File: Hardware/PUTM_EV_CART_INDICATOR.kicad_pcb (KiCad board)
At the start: 2 copper layers, 43 x 25 mm, 17 parts, among them J1 Screw_Terminal_01x08, K3 IM07DTS, K4 IM07DTS

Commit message: poprawy diod
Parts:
- moved D1 10.8 mm to (112.0, 72.0), turned to 0 degrees
- moved D2 6.40 mm to (102.0, 72.0), turned to 0 degrees
- moved K4 1.80 mm to (111.9, 79.3), turned to -90 degrees
- moved K3 1.60 mm to (101.9, 79.1)
- moved H1 1.00 mm to (85.0, 80.0)
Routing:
- net Net-(D1-A): track 16.0 -> 8.33 mm
- net Net-(K4-NC_2): track 11.0 -> 4.48 mm
- net +24V: track 49.4 -> 51.5 mm
- net Net-(D2-A): track 13.0 -> 14.6 mm, vias 0 -> 1
- net Net-(K3-NO_1): track 3.87 -> 5.11 mm
- net /TSAL_COLUMN: track 33.5 -> 34.1 mm
- net /IMD_COLUMN: track 18.8 -> 18.2 mm
- net GND: vias 8 -> 12
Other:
- board size 43 x 25 mm -> 43 x 26.5 mm

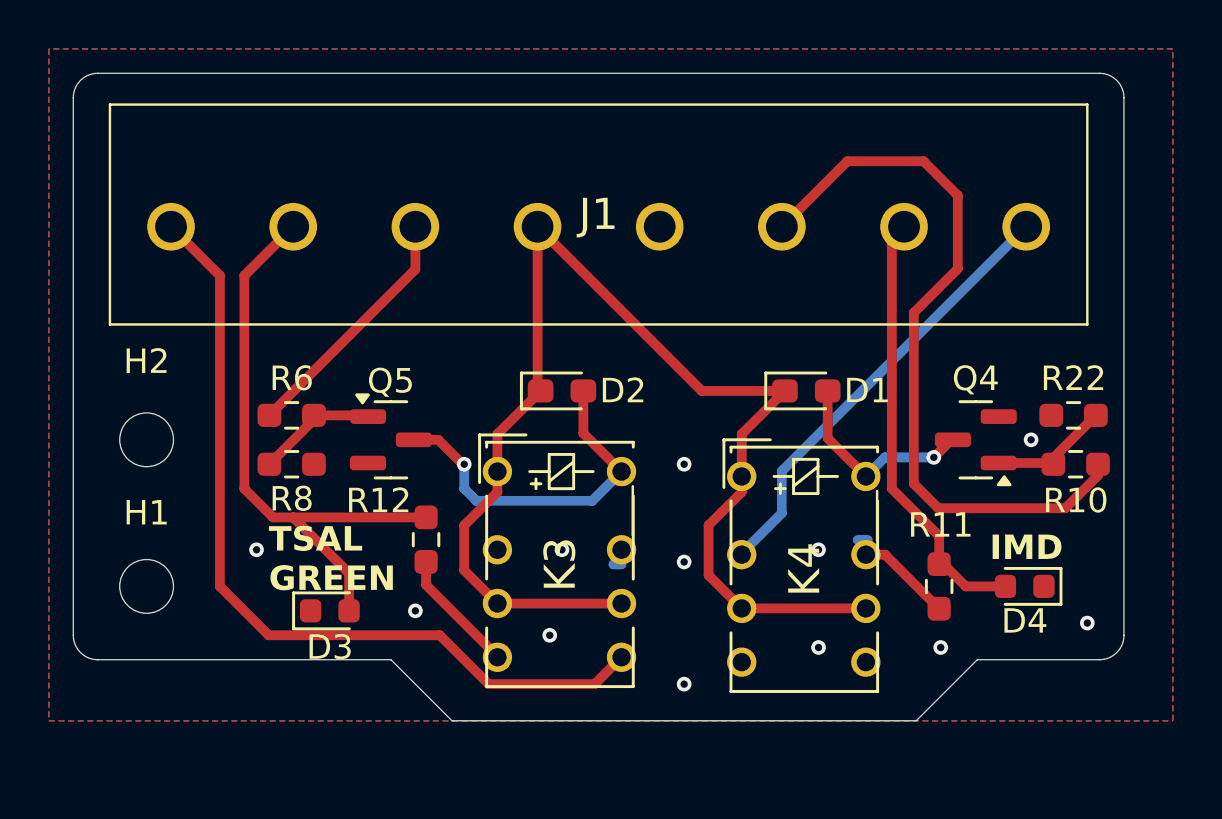
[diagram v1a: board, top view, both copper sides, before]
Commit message: melted tracks
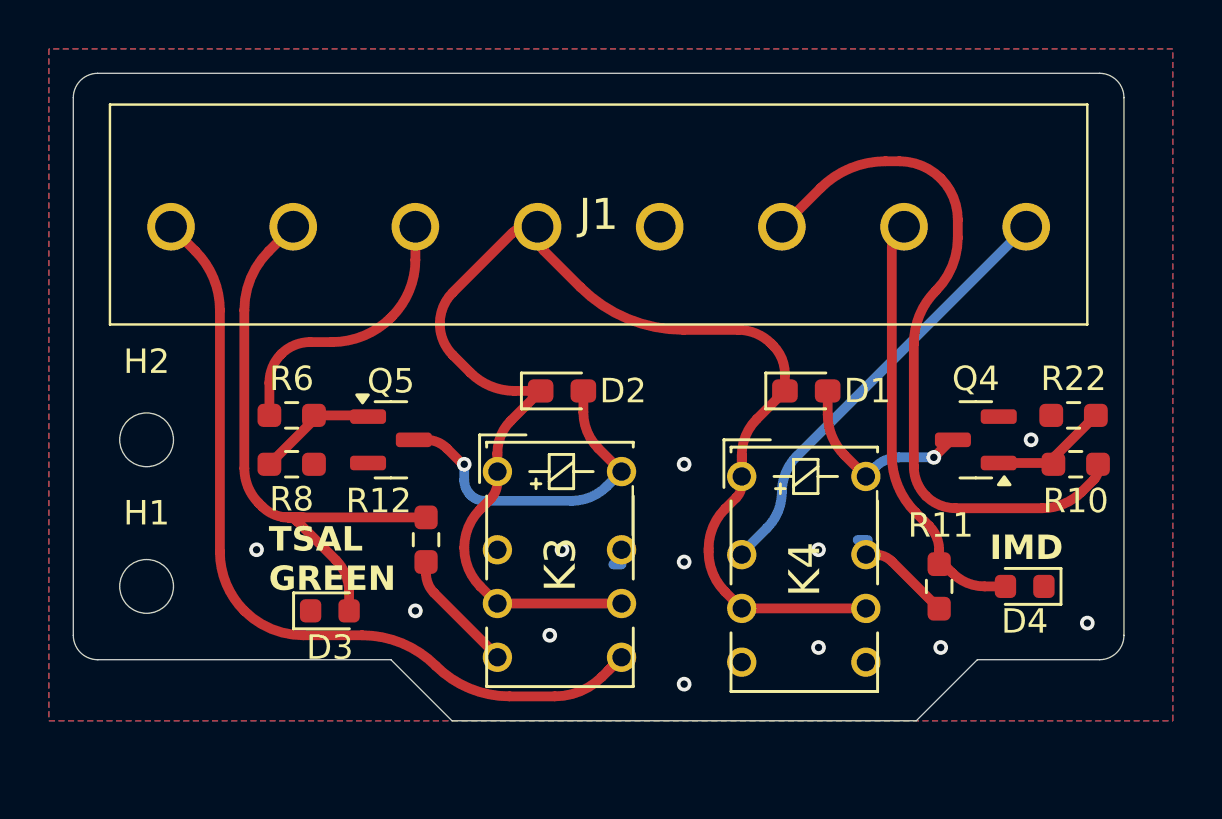
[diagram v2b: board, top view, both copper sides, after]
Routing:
- net +24V: track 51.5 -> 56.2 mm
- net /TSAL_GREEN: track 10.2 -> 11.5 mm
- net /IMD: track 30.4 -> 29.4 mm
- net /TSAL_LED: track 24.2 -> 25.0 mm
- net /TSAL_COLUMN: track 34.1 -> 33.5 mm

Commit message: dodano otwory po drugiej stronie
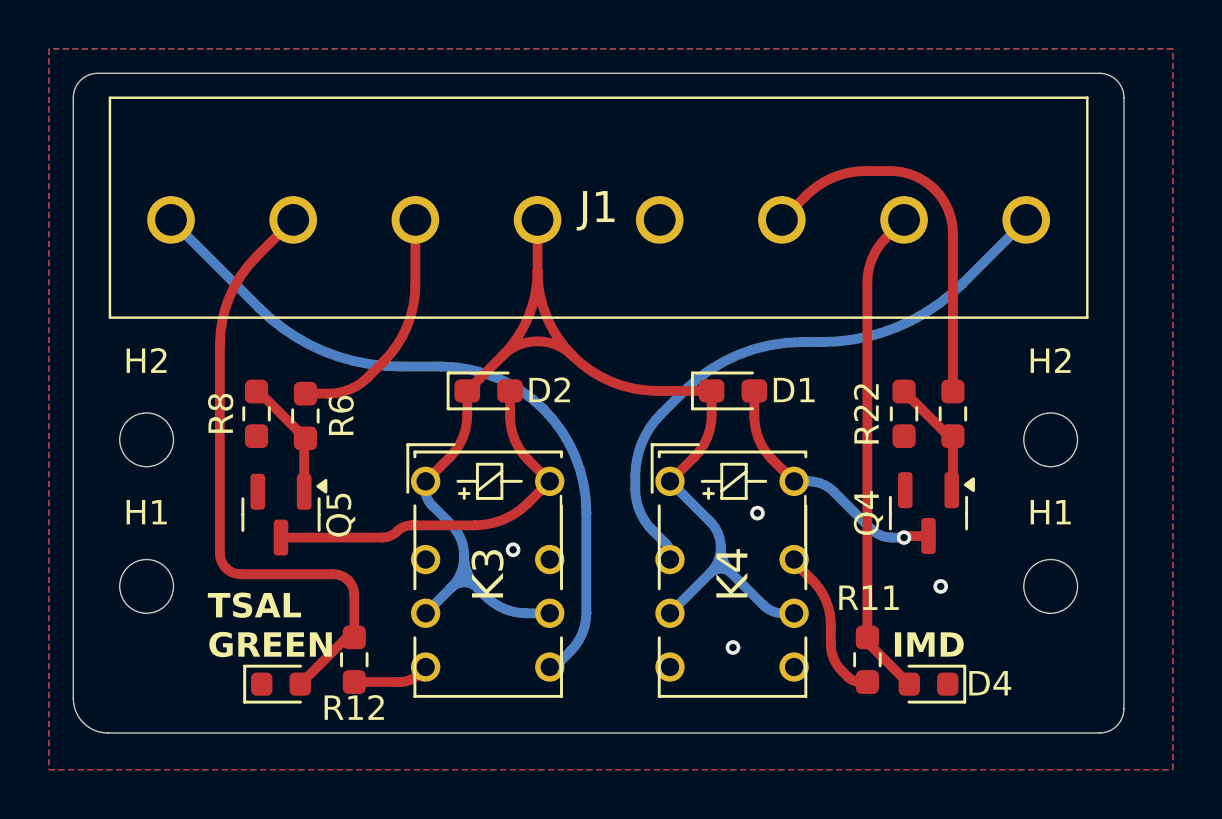
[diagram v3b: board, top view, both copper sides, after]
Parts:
- added H1: MountingHole, MountingHole:MountingHole_2.2mm_M2, F.Cu at (122.0, 80.0)
- added H2: MountingHole, MountingHole:MountingHole_2.2mm_M2, F.Cu at (122.0, 74.0)
- moved R22 6.94 mm to (116.0, 72.9), turned to -90 degrees
- moved R12 5.72 mm to (93.5, 83.0)
- moved D4 5.61 mm to (117.0, 84.0)
- moved Q5 5.44 mm to (90.5, 77.1), turned to -90 degrees
- moved R10 5.43 mm to (118.0, 72.9), turned to 90 degrees
- moved R11 4.20 mm to (114.5, 83.0)
- moved D3 3.61 mm to (90.5, 84.0)
- moved Q4 3.57 mm to (117.0, 77.0), turned to -90 degrees
- moved D1 3.00 mm to (109.0, 72.0)
- moved D2 3.00 mm to (99.0, 72.0)
- moved K3 2.96 mm to (99.0, 79.5)
- moved K4 2.94 mm to (109.0, 79.5)
- moved R8 2.51 mm to (89.5, 72.9), turned to 90 degrees
- moved R6 0.56 mm to (91.5, 73.0), turned to 90 degrees
- moved J1 0.28 mm to (86.0, 65.0)
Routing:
- net /IMD: track 29.4 -> 15.6 mm
- net /IMD_COLUMN: track 18.0 -> 24.2 mm
- net /TSAL_COLUMN: track 33.5 -> 29.4 mm
- net /IMD_LED: track 17.6 -> 20.2 mm
- net Net-(D1-A): track 8.15 -> 10.6 mm
- net +24V: track 56.2 -> 54.2 mm
- net Net-(K4-NC_2): track 4.43 -> 6.36 mm
- net Net-(K3-NO_1): track 5.05 -> 3.12 mm
- net Net-(D2-A): track 14.2 -> 16.0 mm, vias 1 -> 0
- net /TSAL_GREEN: track 11.5 -> 9.76 mm
- net /TSAL_LED: track 25.0 -> 25.8 mm
- net GND: vias 12 -> 4
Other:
- board size 43 x 26.5 mm -> 43 x 27 mm
- board text added: "Krzysiu Ch*** faktury oddawaj"
